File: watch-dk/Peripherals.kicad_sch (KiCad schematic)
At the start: 49 parts, among them IC201 APDS-9306-065, IC202 RV-8263-C8, IC203 BMI270, IC204 LIS2MDLTR, IC205 BMP581, IC206 DRV2603RUNT, J201 Jumper, J202 Jumper, J203 Jumper, J204 Jumper, J205 Jumper, J206 Jumper, M201 Vibrator DC Motor, Q201 DMG1013UW-7, Q202 PMZ550UNEYL, Q203 PMZ550UNEYL, X201 Power, X202 I2S, X203 Power, X204 I2C, X205 Power, X206 Power, X207 Power, X208 Power, X209 Power, X210 Motor

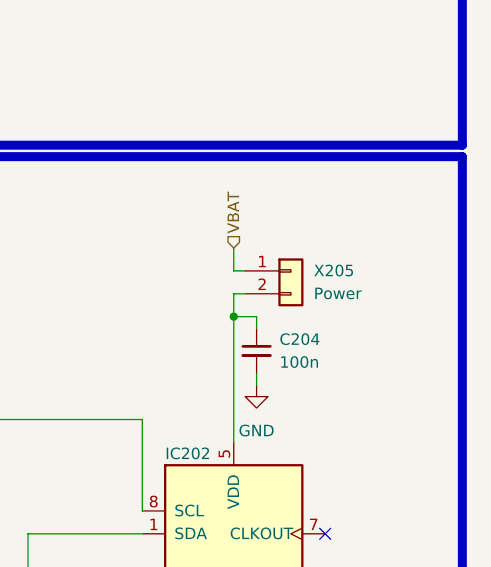
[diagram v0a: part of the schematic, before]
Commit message: Bug: Issue #127
Signed-off-by: Daniel Kampert <DanielKampert@kampis-elektroecke.de>
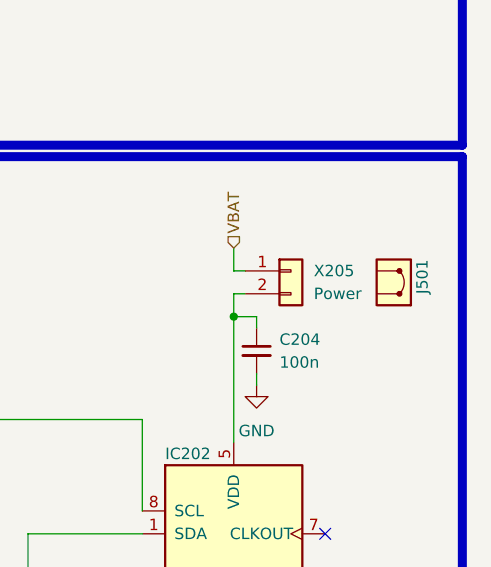
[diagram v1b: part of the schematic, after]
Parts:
- added J501: Jumper, symbol Misc:Jumper
- R201: mouser# RC0402FR-07150KL -> 603-RC0402FR-07150KL
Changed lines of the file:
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@@
 	)
 	(symbol
+		(lib_id "Misc:Jumper")
+		(at 398.78 106.68 180)
+		(unit 1)
+		(exclude_from_sim no)
+		(in_bom yes)
+		(on_board no)
+		(dnp no)
+		(property "Reference" "J501"
+			(at 401.955 104.14 90)
+			(effects
+				(font
+					(size 1.27 1.27)
+				)
+				(justify left)
+			)
+		)
+		(property "Value" "Jumper"
+			(at 396.24 105.4101 0)
+			(effects
+				(font
+					(size 1.27 1.27)
+				)
+				(justify left)
+				(hide yes)
+			)
+		)
+		(property "Footprint" ""
+			(at 398.78 106.68 0)
+			(effects
+				(font
+					(size 1.27 1.27)
+				)
+				(hide yes)
+			)
+		)
+		(property "Datasheet" "https://www.we-online.com/katalog/datasheet/60900213421.pdf"
+			(at 398.78 106.68 0)
+			(effects
+				(font
+					(size 1.27 1.27)
+				)
+				(hide yes)
+			)
+		)
+		(property "Description" "Generic jumper cap"
+			(at 398.78 106.68 0)
+			(effects
+				(font
+					(size 1.27 1.27)
+				)
+				(hide yes)
+			)
+		)
+		(property "manf" " Würth Elektronik"
+			(at 398.78 106.68 0)
+			(effects
+				(font
+					(size 1.27 1.27)
+				)
+				(hide yes)
+			)
+		)
+		(property "manf#" "60900213421"
+			(at 398.78 106.68 0)
+			(effects
+				(font
+					(size 1.27 1.27)
+				)
+				(hide yes)
+			)
+		)
+		(property "mouser#" "710-60900213421"
+			(at 398.78 106.68 0)
+			(effects
+				(font
+					(size 1.27 1.27)
+				)
+				(hide yes)
+			)
+		)
+		(property "CONFIG" ""
+			(at 398.78 106.68 0)
+			(effects
+				(font
+					(size 1.27 1.27)
+				)
+				(hide yes)
+			)
+		)
+		(instances
+			(project "Watch-DK"
+				(path "/d5742f03-3b1a-42e5-a384-018bd4b919aa/c5103ceb-5325-4a84-a025-9638a412984e/82af773f-8c39-43b9-baa2-3658da6c8bb2"
+					(reference "J501")
+					(unit 1)
+				)
+			)
+		)
+	)
+	(symbol
 		(lib_id "Device:C_Small")
 		(at 265.43 135.89 0)
@@
 			)
 		)
-		(property "mouser#" "RC0402FR-07150KL"
+		(property "mouser#" "603-RC0402FR-07150KL"
 			(at 77.47 95.25 0)
 			(effects

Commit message: Task: Issue #129
Signed-off-by: Daniel Kampert <DanielKampert@kampis-elektroecke.de>
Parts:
- X201, X203, X205, X206, X207, X208, X209: value Power -> Current
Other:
- moved on the sheet: J201, J202, J203, J204, J205, J206, J501

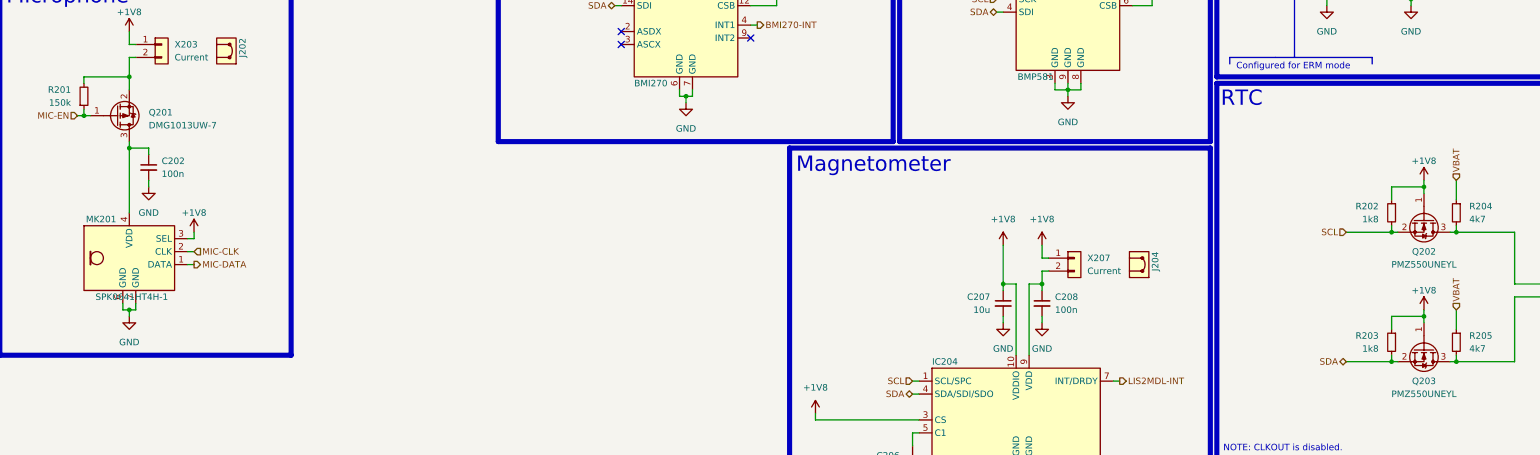
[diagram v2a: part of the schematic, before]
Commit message: Task: Issue #130
Signed-off-by: Daniel Kampert <DanielKampert@kampis-elektroecke.de>
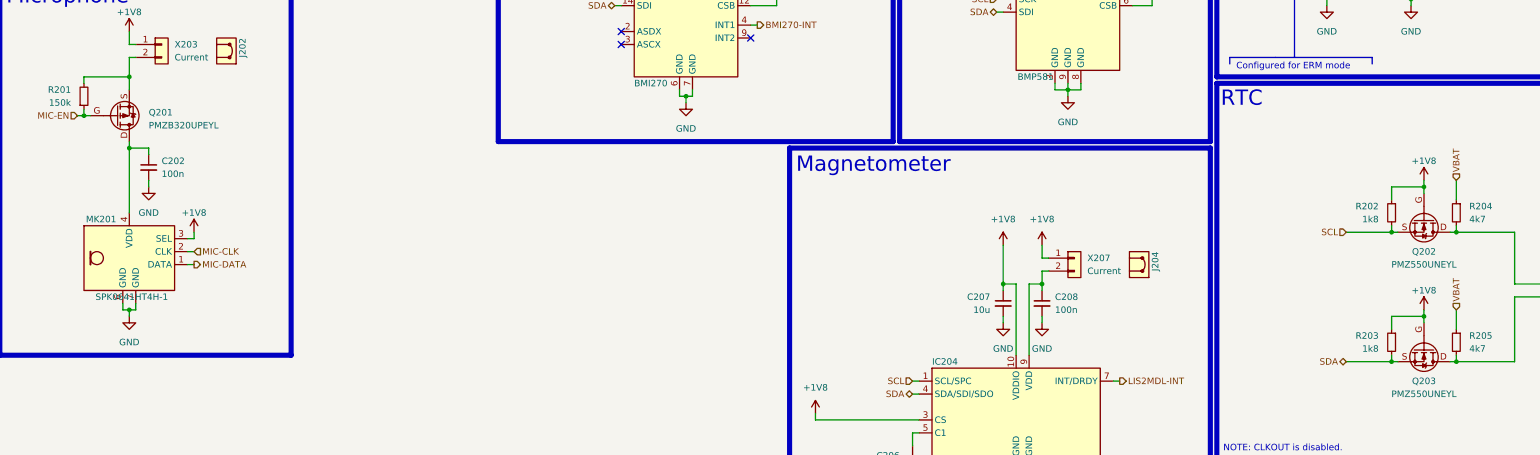
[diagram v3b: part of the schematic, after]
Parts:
- removed Q201: DMG1013UW-7, Package_TO_SOT_SMD:SOT-323_SC-70, symbol Diodes Incorporated:DMG1013UW-7
- added Q201: PMZB320UPEYL, Package_DFN_Kampi:DFN-1006-3, symbol Nexperia:PMZB320UPE
- Q202, Q203: footprint Package_SOT_SMD:SOT-883 -> Package_DFN_Kampi:DFN-1006-3; symbol Nexperia:PMZ550UNEYL -> Nexperia:PMZ550UNE
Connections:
- net +1V8: now also Q202.G, Q203.G; no longer Q202.1 (G), Q203.1 (G)
- net MIC-EN: now also Q201.G
- net SCL: now also Q202.S; no longer Q202.2 (S)
- net SDA: now also Q203.S; no longer Q203.2 (S)
- net at IC202.8 (SCL), R204.2: now also Q202.D; no longer Q202.3 (D)
- net at IC202.1 (SDA), R205.2: now also Q203.D; no longer Q203.3 (D)
- net at R201.2, X203.2 (Pin_2): now also Q201.S
- net at C202.1, MK201.4 (VDD): now also Q201.D
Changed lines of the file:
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@@
 	)
 	(symbol
-		(lib_id "Nexperia:PMZ550UNEYL")
+		(lib_id "Nexperia:PMZ550UNE")
 		(at 340.36 119.38 270)
 		(unit 1)
@@
 			)
 		)
-		(property "Footprint" "Package_SOT_SMD:SOT-883"
-			(at 338.455 124.46 0)
+		(property "Footprint" "Package_DFN_Kampi:DFN-1006-3"
+			(at 340.36 119.38 0)
 			(effects
 				(font
@@
 		)
 		(property "Datasheet" "https://assets.nexperia.com/documents/data-sheet/PMZ550UNE.pdf"
-			(at 336.55 124.46 0)
+			(at 340.36 119.38 0)
 			(effects
 				(font
@@
 			)
 		)
-		(pin "2"
+		(pin "S"
 		)
-		(pin "1"
+		(pin "G"
 		)
-		(pin "3"
+		(pin "D"
 		)
 		(instances
@@
 	)
 	(symbol
+		(lib_id "Nexperia:PMZB320UPE")
+		(at 86.36 99.06 0)
+		(mirror x)
+		(unit 1)
+		(exclude_from_sim no)
+		(in_bom yes)
+		(on_board yes)
+		(dnp no)
+		(property "Reference" "Q201"
+			(at 90.17 98.425 0)
+			(effects
+				(font
+					(size 1.27 1.27)
+				)
+				(justify left)
+			)
+		)
+		(property "Value" "PMZB320UPEYL"
+			(at 90.17 100.965 0)
+			(effects
+				(font
+					(size 1.27 1.27)
+				)
+				(justify left)
+			)
+		)
+		(property "Footprint" "Package_DFN_Kampi:DFN-1006-3"
+			(at 73.66 99.06 0)
+			(effects
+				(font
+					(size 1.27 1.27)
+				)
+				(justify left)
+				(hide yes)
+			)
+		)
+		(property "Datasheet" "https://assets.nexperia.com/documents/data-sheet/PMZB320UPE.pdf"
+			(at 72.39 99.06 0)
+			(effects
+				(font
+					(size 1.27 1.27)
+				)
+				(justify left)
+				(hide yes)
+			)
+		)
+		(property "Description" "1A Id, 30V Vds"
+			(at 86.36 99.06 0)
+			(effects
+				(font
+					(size 1.27 1.27)
+				)
+				(hide yes)
+			)
+		)
+		(property "CONFIG" ""
+			(at 86.36 99.06 0)
+			(effects
+				(font
+					(size 1.27 1.27)
+				)
+				(hide yes)
+			)
+		)
+		(property "manf" "ROHM Semiconductor"
+			(at 86.36 99.06 0)
+			(effects
+				(font
+					(size 1.27 1.27)
+				)
+				(hide yes)
+			)
+		)
+		(property "manf#" "PMZB320UPEYL"
+			(at 86.36 99.06 0)
+			(effects
+				(font
+					(size 1.27 1.27)
+				)
+				(hide yes)
+			)
+		)
+		(property "mouser#" "771-PMZB320UPEYL"
+			(at 86.36 99.06 0)
+			(effects
+				(font
+					(size 1.27 1.27)
+				)
+				(hide yes)
+			)
+		)
+		(pin "S"
+		)
+		(pin "D"
+		)
+		(pin "G"
+		)
+		(instances
+			(project "Watch-DK"
+				(path "/d5742f03-3b1a-42e5-a384-018bd4b919aa/c5103ceb-5325-4a84-a025-9638a412984e/82af773f-8c39-43b9-baa2-3658da6c8bb2"
+					(reference "Q201")
+					(unit 1)
+				)
+			)
+		)
+	)
+	(symbol
 		(lib_id "power:+1V8")
 		(at 274.32 35.56 0)
@@
 	)
 	(symbol
-		(lib_id "Diodes Incorporated:DMG1013UW-7")
-		(at 86.36 99.06 0)
-		(mirror x)
-		(unit 1)
-		(exclude_from_sim no)
-		(in_bom yes)
-		(on_board yes)
-		(dnp no)
-		(property "Reference" "Q201"
-			(at 90.17 98.425 0)
-			(effects
-				(font
-					(size 1.27 1.27)
-				)
-				(justify left)
-			)
-		)
-		(property "Value" "DMG1013UW-7"
-			(at 90.17 100.965 0)
-			(effects
-				(font
-					(size 1.27 1.27)
-				)
-				(justify left)
-			)
-		)
-		(property "Footprint" "Package_TO_SOT_SMD:SOT-323_SC-70"
-			(at 73.66 99.06 0)
-			(effects
-				(font
-					(size 1.27 1.27)
-				)
-				(justify left)
-				(hide yes)
-			)
-		)
-		(property "Datasheet" "https://www.diodes.com/assets/Datasheets/ds31861.pdf"
-			(at 72.39 99.06 0)
-			(effects
-				(font
-					(size 1.27 1.27)
-				)
-				(justify left)
-				(hide yes)
-			)
-		)
-		(property "Description" ""
-			(at 86.36 99.06 0)
-			(effects
-				(font
-					(size 1.27 1.27)
-				)
-				(hide yes)
-			)
-		)
-		(property "CONFIG" ""
-			(at 86.36 99.06 0)
-			(effects
-				(font
-					(size 1.27 1.27)
-				)
-				(hide yes)
-			)
-		)
-		(property "manf" "ROHM Semiconductor"
-			(at 86.36 99.06 0)
-			(effects
-				(font
-					(size 1.27 1.27)
-				)
-				(hide yes)
-			)
-		)
-		(property "manf#" "DMG1013UW-7"
-			(at 86.36 99.06 0)
-			(effects
-				(font
-					(size 1.27 1.27)
-				)
-				(hide yes)
-			)
-		)
-		(property "mouser#" "621-DMG1013UW-7"
-			(at 86.36 99.06 0)
-			(effects
-				(font
-					(size 1.27 1.27)
-				)
-				(hide yes)
-			)
-		)
-		(pin "1"
-		)
-		(pin "2"
-		)
-		(pin "3"
-		)
-		(instances
-			(project "Dev-Kit"
-				(path "/d5742f03-3b1a-42e5-a384-018bd4b919aa/c5103ceb-5325-4a84-a025-9638a412984e/82af773f-8c39-43b9-baa2-3658da6c8bb2"
-					(reference "Q201")
-					(unit 1)
-				)
-			)
-		)
-	)
-	(symbol
 		(lib_id "Sensor_Optical:APDS-9306-065")
 		(at 30.48 54.61 0)
@@
 	)
 	(symbol
-		(lib_id "Nexperia:PMZ550UNEYL")
+		(lib_id "Nexperia:PMZ550UNE")
 		(at 340.36 144.78 270)
 		(unit 1)
@@
 			)
 		)
-		(property "Footprint" "Package_SOT_SMD:SOT-883"
-			(at 338.455 149.86 0)
+		(property "Footprint" "Package_DFN_Kampi:DFN-1006-3"
+			(at 340.36 144.78 0)
 			(effects
 				(font
@@
 		)
 		(property "Datasheet" "https://assets.nexperia.com/documents/data-sheet/PMZ550UNE.pdf"
-			(at 336.55 149.86 0)
+			(at 340.36 144.78 0)
 			(effects
 				(font
@@
 			)
 		)
-		(pin "2"
+		(pin "D"
 		)
-		(pin "1"
+		(pin "G"
 		)
-		(pin "3"
+		(pin "S"
 		)
 		(instances

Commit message: Feature: Issue #131
- Fix wrong page numbers
- Update reference designators to match the page numbers

Signed-off-by: Daniel Kampert <DanielKampert@kampis-elektroecke.de>
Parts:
- renumbered C201 to C501, C202 to C502, C203 to C503, C205 to C504, C206 to C505, C207 to C506, C208 to C507, C209 to C508, C210 to C509, C211 to C510, C204 to C511, IC201 to IC501, IC203 to IC502, IC204 to IC503, IC205 to IC504, IC206 to IC505, IC202 to IC506, J201 to J501, J202 to J502, J203 to J503, J204 to J504, J205 to J505, J206 to J506, J501 to J507, M201 to M501, MK201 to MK501, Q201 to Q501, Q202 to Q502, Q203 to Q503, R201 to R501, R202 to R502, R203 to R503, R204 to R504, R205 to R505, S201 to S501, S202 to S502, S203 to S503, S204 to S504, TP201 to TP501, TP202 to TP502, X201 to X501, X202 to X502, X203 to X503, X204 to X504, X206 to X505, X207 to X506, X208 to X507, X209 to X508, X210 to X509, X205 to X510

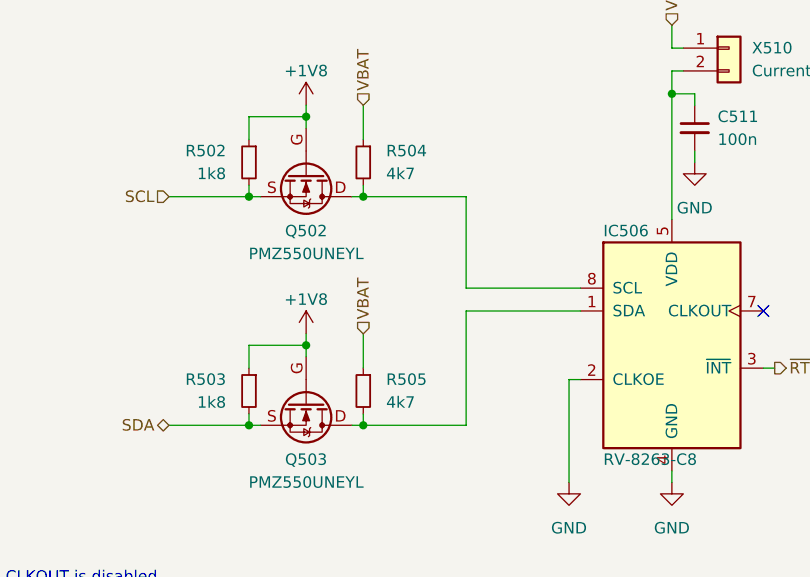
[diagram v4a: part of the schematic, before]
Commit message: Bug: Issue #132
Signed-off-by: Daniel Kampert <DanielKampert@kampis-elektroecke.de>
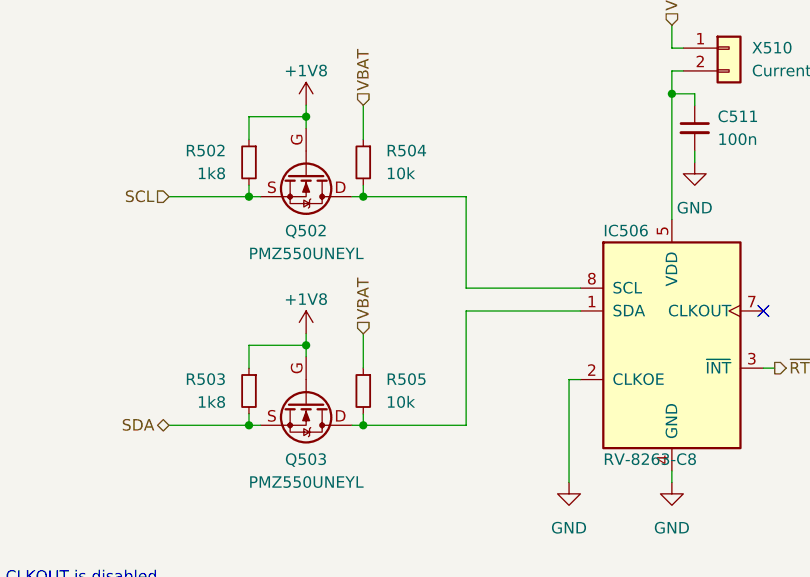
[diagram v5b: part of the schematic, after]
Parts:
- R504, R505: value 4k7 -> 10k; manf# RC0402FR-074K7L -> RC0402FR-0710KL; mouser# 603-RC0402FR-074K7L -> 603-RC0402FR-0710KL
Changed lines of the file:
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@@
 			)
 		)
-		(property "Value" "4k7"
+		(property "Value" "10k"
 			(at 349.25 144.7799 0)
 			(effects
@@
 			)
 		)
-		(property "manf#" "RC0402FR-074K7L"
+		(property "manf#" "RC0402FR-0710KL"
 			(at 346.71 143.51 0)
 			(effects
@@
 			)
 		)
-		(property "mouser#" "603-RC0402FR-074K7L"
+		(property "mouser#" "603-RC0402FR-0710KL"
 			(at 346.71 143.51 0)
 			(effects
@@
 			)
 		)
-		(property "Value" "4k7"
+		(property "Value" "10k"
 			(at 349.25 119.3799 0)
 			(effects
@@
 			)
 		)
-		(property "manf#" "RC0402FR-074K7L"
+		(property "manf#" "RC0402FR-0710KL"
 			(at 346.71 118.11 0)
 			(effects
@@
 			)
 		)
-		(property "mouser#" "603-RC0402FR-074K7L"
+		(property "mouser#" "603-RC0402FR-0710KL"
 			(at 346.71 118.11 0)
 			(effects

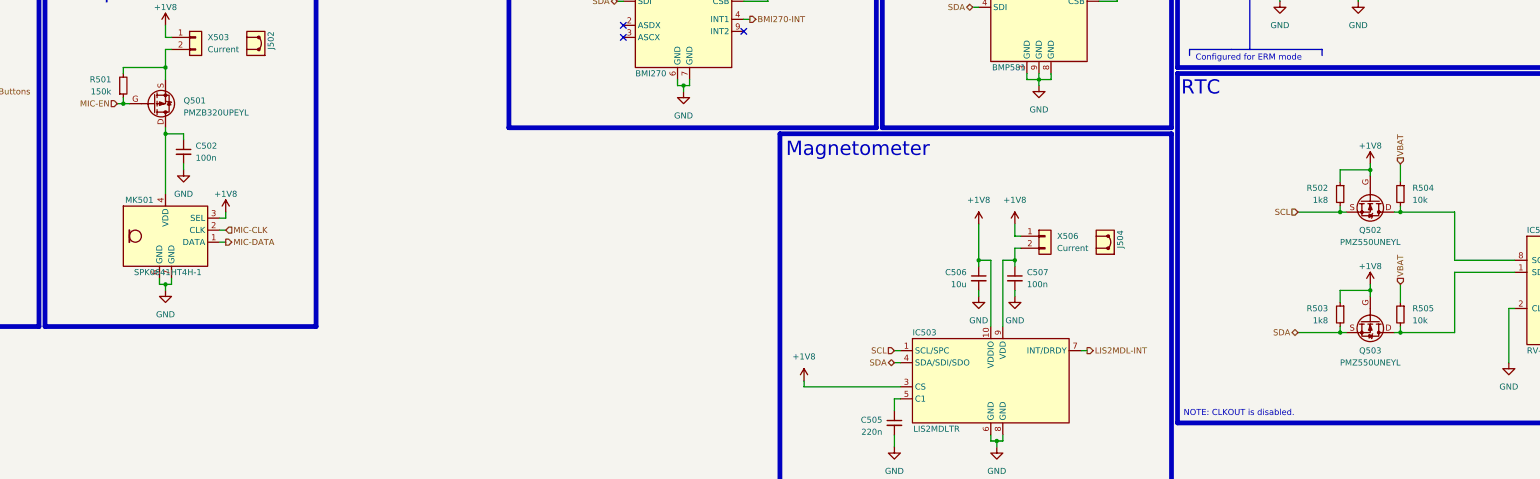
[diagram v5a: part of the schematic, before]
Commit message: Feature: Issue #133
Signed-off-by: Daniel Kampert <DanielKampert@kampis-elektroecke.de>
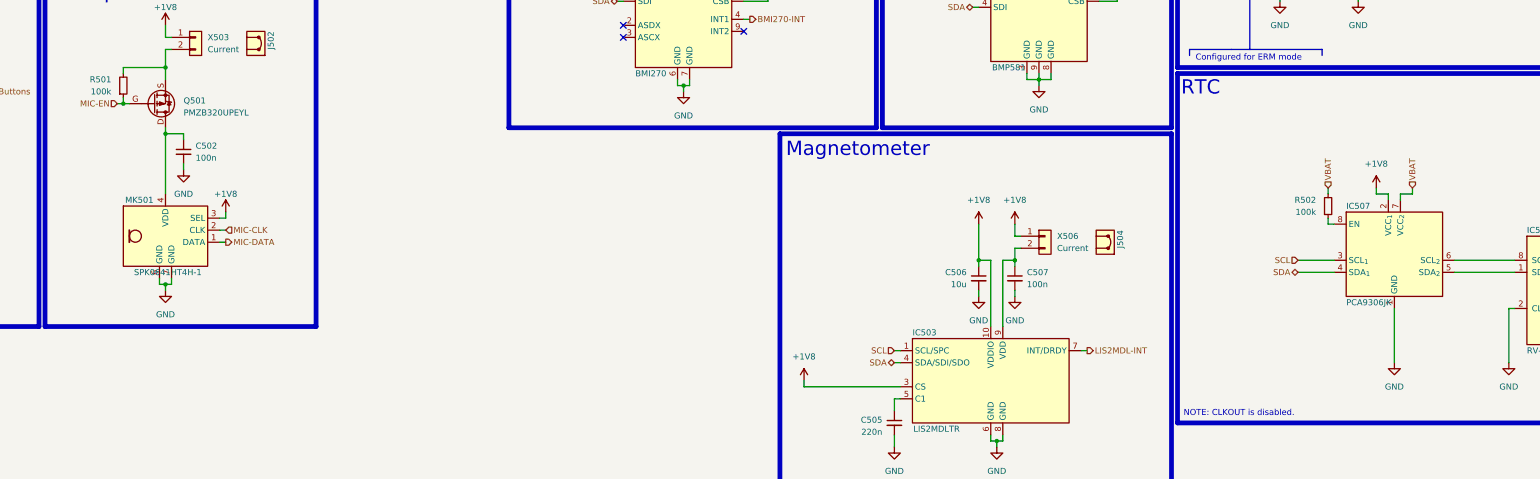
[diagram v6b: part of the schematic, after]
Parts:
- removed Q502, Q503: PMZ550UNEYL, Package_DFN_Kampi:DFN-1006-3, symbol Nexperia:PMZ550UNE
- removed R503: 1k8, Resistor_SMD:R_0402_1005Metric, symbol Device:R_Small
- removed R504, R505: 10k, Resistor_SMD:R_0402_1005Metric, symbol Device:R_Small
- added IC507: PCA9306JK, https://www.nxp.com/docs/en/data-sheet/PCA9306.pdf, symbol NXP:PCA9306JK
- R501: value 150k -> 100k; manf# RC0402FR-07150KL -> RC0404FR-07100KL; mouser# 603-RC0402FR-07150KL -> 603-RC0404FR-07100KL
- R502: value 1k8 -> 100k; manf# RC0402FR-071K8L -> RC0404FR-07100KL; mouser# 603-RC0402FR-071K8L -> 603-RC0404FR-07100KL
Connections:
- net +1V8: now also IC507.2 (VCC_{1}); no longer R502.1
- net GND: now also IC507.1 (GND)
- net SCL: now also IC507.3 (SCL_{1}); no longer R502.2
- net SDA: now also IC507.4 (SDA_{1})
- net VBAT: now also R502.2, IC507.7 (VCC_{2})
- net at IC506.8 (SCL): now also IC507.6 (SCL_{2})
- net at IC506.1 (SDA): now also IC507.5 (SDA_{2})
- new net: IC507.8 (EN), R502.1
